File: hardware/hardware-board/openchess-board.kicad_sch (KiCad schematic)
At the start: 243 parts, among them J1 Conn_02x13, U1 DRV5032FC, U10 DRV5032FC, U11 DRV5032FC, U12 DRV5032FC, U13 DRV5032FC, U14 DRV5032FC, U15 DRV5032FC, U16 DRV5032FC, U17 DRV5032FC, U18 DRV5032FC, U19 DRV5032FC, U2 DRV5032FC, U20 DRV5032FC, U21 DRV5032FC, U22 DRV5032FC, U23 DRV5032FC, U24 DRV5032FC, U25 DRV5032FC, U26 DRV5032FC, U27 DRV5032FC, U28 DRV5032FC, U29 DRV5032FC, U3 DRV5032FC, U30 DRV5032FC, U31 DRV5032FC, U32 DRV5032FC, U33 DRV5032FC, U34 DRV5032FC, U35 DRV5032FC, U36 DRV5032FC, U37 DRV5032FC, U38 DRV5032FC, U39 DRV5032FC, U4 DRV5032FC, U40 DRV5032FC, U41 DRV5032FC, U42 DRV5032FC, U43 DRV5032FC, U44 DRV5032FC, U45 DRV5032FC, U46 DRV5032FC, U47 DRV5032FC, U48 DRV5032FC, U49 DRV5032FC, U5 DRV5032FC, U50 DRV5032FC, U51 DRV5032FC, U52 DRV5032FC, U53 DRV5032FC, U54 DRV5032FC, U55 DRV5032FC, U56 DRV5032FC, U57 DRV5032FC, U58 DRV5032FC, U59 DRV5032FC, U6 DRV5032FC, U60 DRV5032FC, U61 DRV5032FC, U62 DRV5032FC, U63 DRV5032FC, U64 DRV5032FC, U7 DRV5032FC, U8 DRV5032FC, U9 DRV5032FC

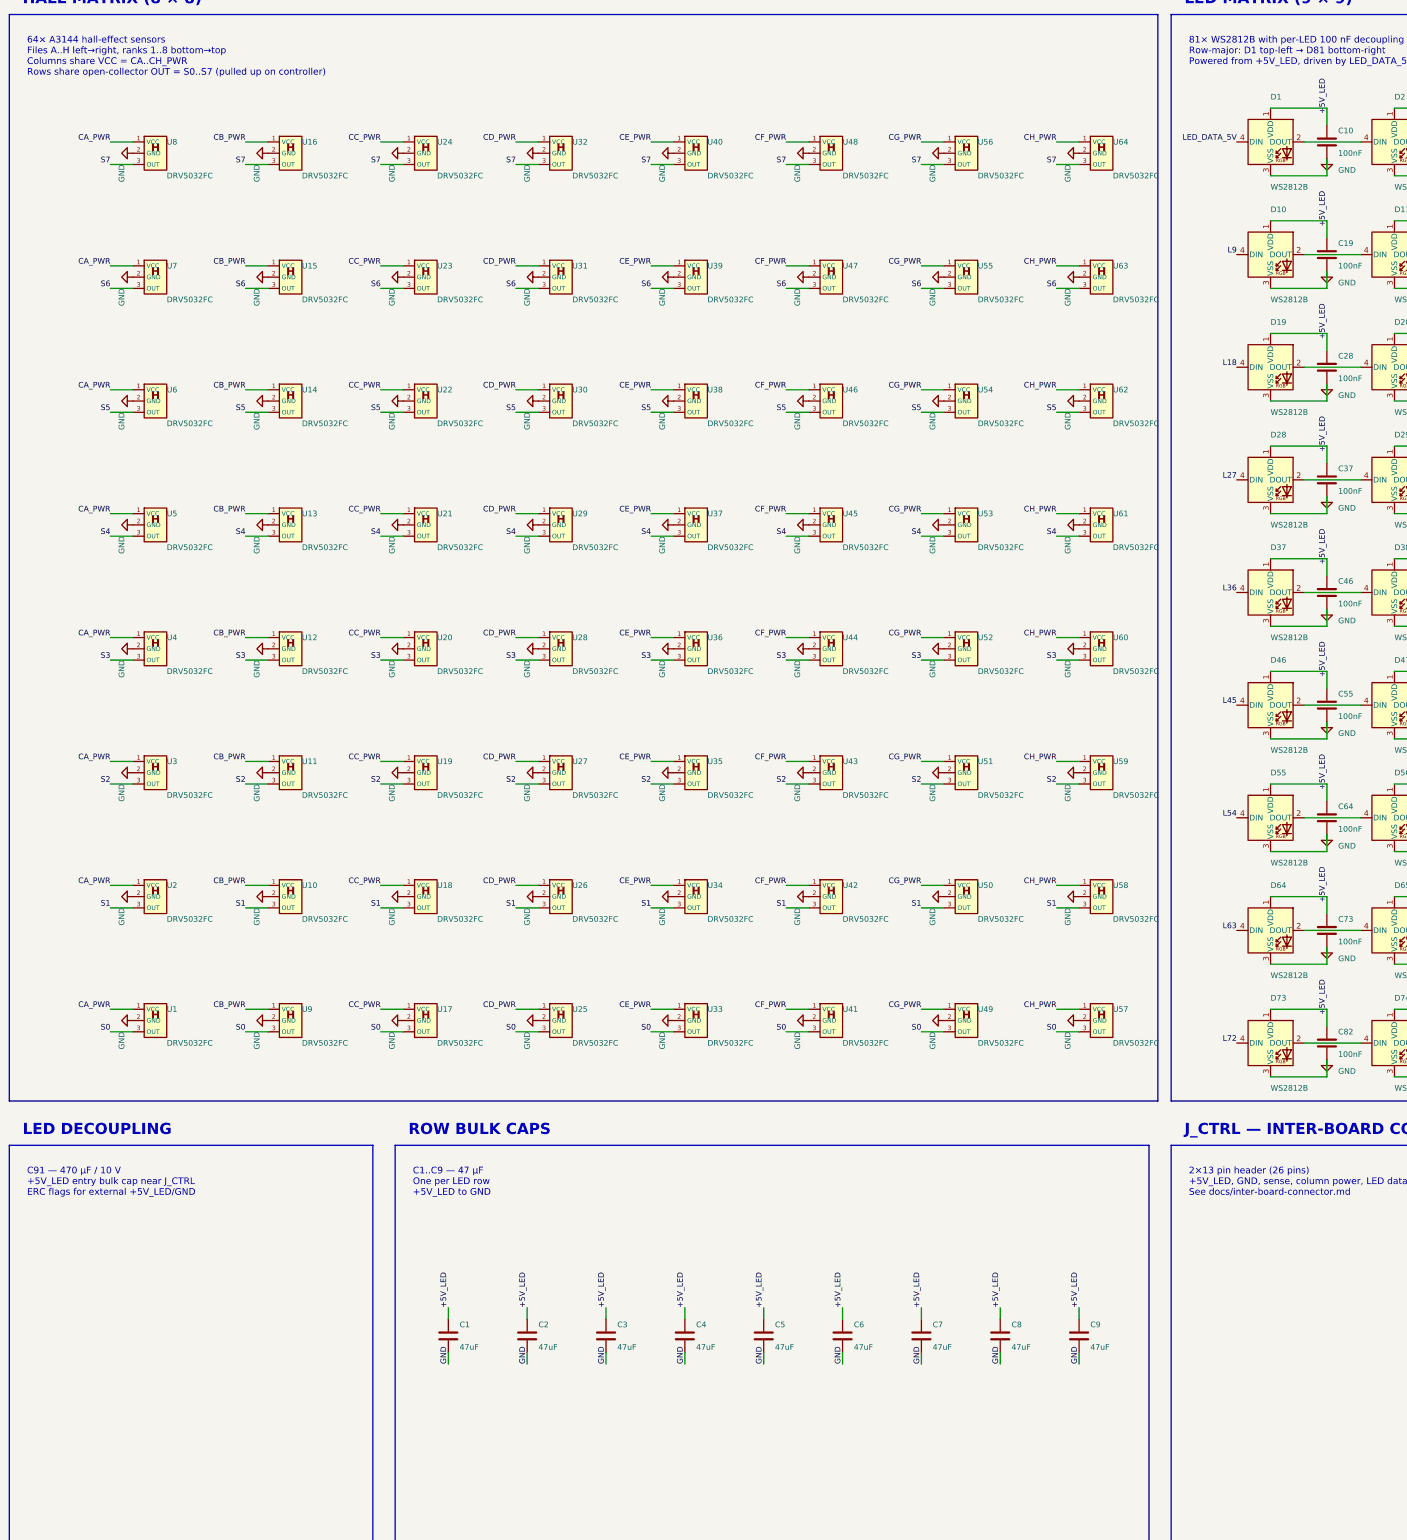
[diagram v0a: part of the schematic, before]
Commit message: Add initial positions CSV for hardware components
This commit introduces a new CSV file containing the designator, midpoints, rotation, and layer information for various hardware components used in the project. The data includes positions for capacitors, resistors, diodes, and connectors, which are essential for the assembly and layout of the hardware.
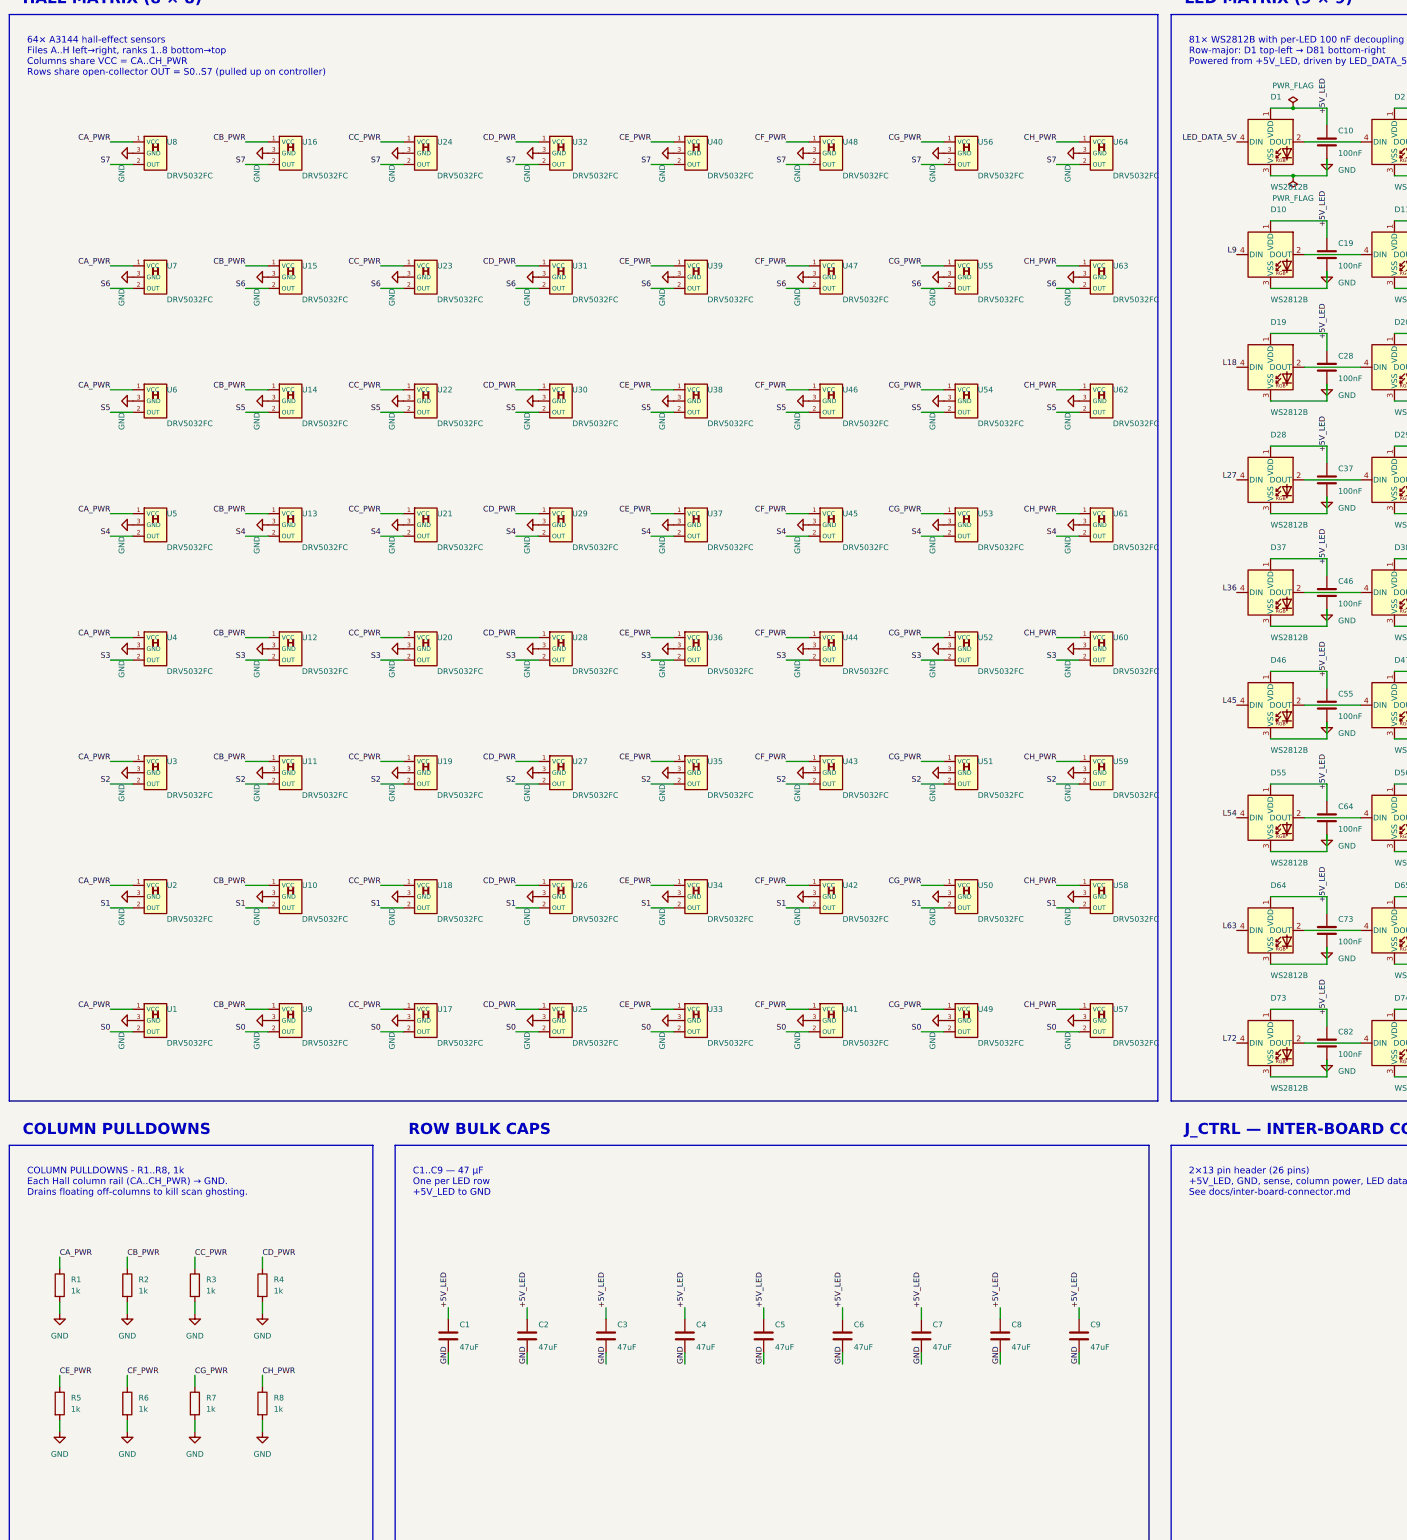
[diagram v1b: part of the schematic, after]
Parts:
- added R1, R2, R3, R4, R5, R6, R7, R8: 1k, Resistor_SMD:R_0805_2012Metric_Pad1.20x1.40mm_HandSolder, symbol Device:R
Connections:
- net CA_PWR: now also R1.1
- net CB_PWR: now also R2.1
- net CC_PWR: now also R3.1
- net CD_PWR: now also R4.1
- net CE_PWR: now also R5.1
- net CF_PWR: now also R6.1
- net CG_PWR: now also R7.1
- net CH_PWR: now also R8.1
- net GND: now also U1.3 (GND), U10.3 (GND), U11.3 (GND), U12.3 (GND), U13.3 (GND), U14.3 (GND), U15.3 (GND), U16.3 (GND), U17.3 (GND), U18.3 (GND), U19.3 (GND), U2.3 (GND), U20.3 (GND), U21.3 (GND), U22.3 (GND), U23.3 (GND), U24.3 (GND), U25.3 (GND), U26.3 (GND), U27.3 (GND), U28.3 (GND), U29.3 (GND), U3.3 (GND), U30.3 (GND), U31.3 (GND), U32.3 (GND), U33.3 (GND), U34.3 (GND), U35.3 (GND), U36.3 (GND), U37.3 (GND), U38.3 (GND), U39.3 (GND), U4.3 (GND), U40.3 (GND), U41.3 (GND), U42.3 (GND), U43.3 (GND), U44.3 (GND), U45.3 (GND), U46.3 (GND), U47.3 (GND), U48.3 (GND), U49.3 (GND), U5.3 (GND), U50.3 (GND), U51.3 (GND), U52.3 (GND), U53.3 (GND), U54.3 (GND), U55.3 (GND), U56.3 (GND), U57.3 (GND), U58.3 (GND), U59.3 (GND), U6.3 (GND), U60.3 (GND), U61.3 (GND), U62.3 (GND), U63.3 (GND), U64.3 (GND), U7.3 (GND), U8.3 (GND), U9.3 (GND), R1.2, R2.2, R3.2, R4.2, R5.2, R6.2, R7.2, R8.2; no longer U1.2 (GND), U10.2 (GND), U11.2 (GND), U12.2 (GND), U13.2 (GND), U14.2 (GND), U15.2 (GND), U16.2 (GND), U17.2 (GND), U18.2 (GND), U19.2 (GND), U2.2 (GND), U20.2 (GND), U21.2 (GND), U22.2 (GND), U23.2 (GND), U24.2 (GND), U25.2 (GND), U26.2 (GND), U27.2 (GND), U28.2 (GND), U29.2 (GND), U3.2 (GND), U30.2 (GND), U31.2 (GND), U32.2 (GND), U33.2 (GND), U34.2 (GND), U35.2 (GND), U36.2 (GND), U37.2 (GND), U38.2 (GND), U39.2 (GND), U4.2 (GND), U40.2 (GND), U41.2 (GND), U42.2 (GND), U43.2 (GND), U44.2 (GND), U45.2 (GND), U46.2 (GND), U47.2 (GND), U48.2 (GND), U49.2 (GND), U5.2 (GND), U50.2 (GND), U51.2 (GND), U52.2 (GND), U53.2 (GND), U54.2 (GND), U55.2 (GND), U56.2 (GND), U57.2 (GND), U58.2 (GND), U59.2 (GND), U6.2 (GND), U60.2 (GND), U61.2 (GND), U62.2 (GND), U63.2 (GND), U64.2 (GND), U7.2 (GND), U8.2 (GND), U9.2 (GND)
- net S0: now also U1.2 (OUT), U17.2 (OUT), U25.2 (OUT), U33.2 (OUT), U41.2 (OUT), U49.2 (OUT), U57.2 (OUT), U9.2 (OUT); no longer U1.3 (OUT), U17.3 (OUT), U25.3 (OUT), U33.3 (OUT), U41.3 (OUT), U49.3 (OUT), U57.3 (OUT), U9.3 (OUT)
- net S1: now also U10.2 (OUT), U18.2 (OUT), U2.2 (OUT), U26.2 (OUT), U34.2 (OUT), U42.2 (OUT), U50.2 (OUT), U58.2 (OUT); no longer U10.3 (OUT), U18.3 (OUT), U2.3 (OUT), U26.3 (OUT), U34.3 (OUT), U42.3 (OUT), U50.3 (OUT), U58.3 (OUT)
- net S2: now also U11.2 (OUT), U19.2 (OUT), U27.2 (OUT), U3.2 (OUT), U35.2 (OUT), U43.2 (OUT), U51.2 (OUT), U59.2 (OUT); no longer U11.3 (OUT), U19.3 (OUT), U27.3 (OUT), U3.3 (OUT), U35.3 (OUT), U43.3 (OUT), U51.3 (OUT), U59.3 (OUT)
- net S3: now also U12.2 (OUT), U20.2 (OUT), U28.2 (OUT), U36.2 (OUT), U4.2 (OUT), U44.2 (OUT), U52.2 (OUT), U60.2 (OUT); no longer U12.3 (OUT), U20.3 (OUT), U28.3 (OUT), U36.3 (OUT), U4.3 (OUT), U44.3 (OUT), U52.3 (OUT), U60.3 (OUT)
- net S4: now also U13.2 (OUT), U21.2 (OUT), U29.2 (OUT), U37.2 (OUT), U45.2 (OUT), U5.2 (OUT), U53.2 (OUT), U61.2 (OUT); no longer U13.3 (OUT), U21.3 (OUT), U29.3 (OUT), U37.3 (OUT), U45.3 (OUT), U5.3 (OUT), U53.3 (OUT), U61.3 (OUT)
- net S5: now also U14.2 (OUT), U22.2 (OUT), U30.2 (OUT), U38.2 (OUT), U46.2 (OUT), U54.2 (OUT), U6.2 (OUT), U62.2 (OUT); no longer U14.3 (OUT), U22.3 (OUT), U30.3 (OUT), U38.3 (OUT), U46.3 (OUT), U54.3 (OUT), U6.3 (OUT), U62.3 (OUT)
- net S6: now also U15.2 (OUT), U23.2 (OUT), U31.2 (OUT), U39.2 (OUT), U47.2 (OUT), U55.2 (OUT), U63.2 (OUT), U7.2 (OUT); no longer U15.3 (OUT), U23.3 (OUT), U31.3 (OUT), U39.3 (OUT), U47.3 (OUT), U55.3 (OUT), U63.3 (OUT), U7.3 (OUT)
- net S7: now also U16.2 (OUT), U24.2 (OUT), U32.2 (OUT), U40.2 (OUT), U48.2 (OUT), U56.2 (OUT), U64.2 (OUT), U8.2 (OUT); no longer U16.3 (OUT), U24.3 (OUT), U32.3 (OUT), U40.3 (OUT), U48.3 (OUT), U56.3 (OUT), U64.3 (OUT), U8.3 (OUT)
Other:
- note added: "COLUMN PULLDOWNS"
- note added: "COLUMN PULLDOWNS - R1..R8, 1k Each Hall column rail (CA..CH_PWR) → GND. Drains floating off-columns to kill scan ghosting."
- note removed: "C91 — 470 µF / 10 V +5V_LED entry bulk cap near J_CTRL ERC flags for external +5V_LED/GND"
- note removed: "LED DECOUPLING"
